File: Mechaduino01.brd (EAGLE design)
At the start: 41.9 x 41.9 mm, 70 parts, among them IC1 SAMD21G18A-AUT, IC2 AP2202-ADJ, Q1 2.5A/30V, Q2 NFET, Q3 BSS138, Q4 BSS138, Q5 BSS138, U3 74AHC1G125, Y1 32,768Khz

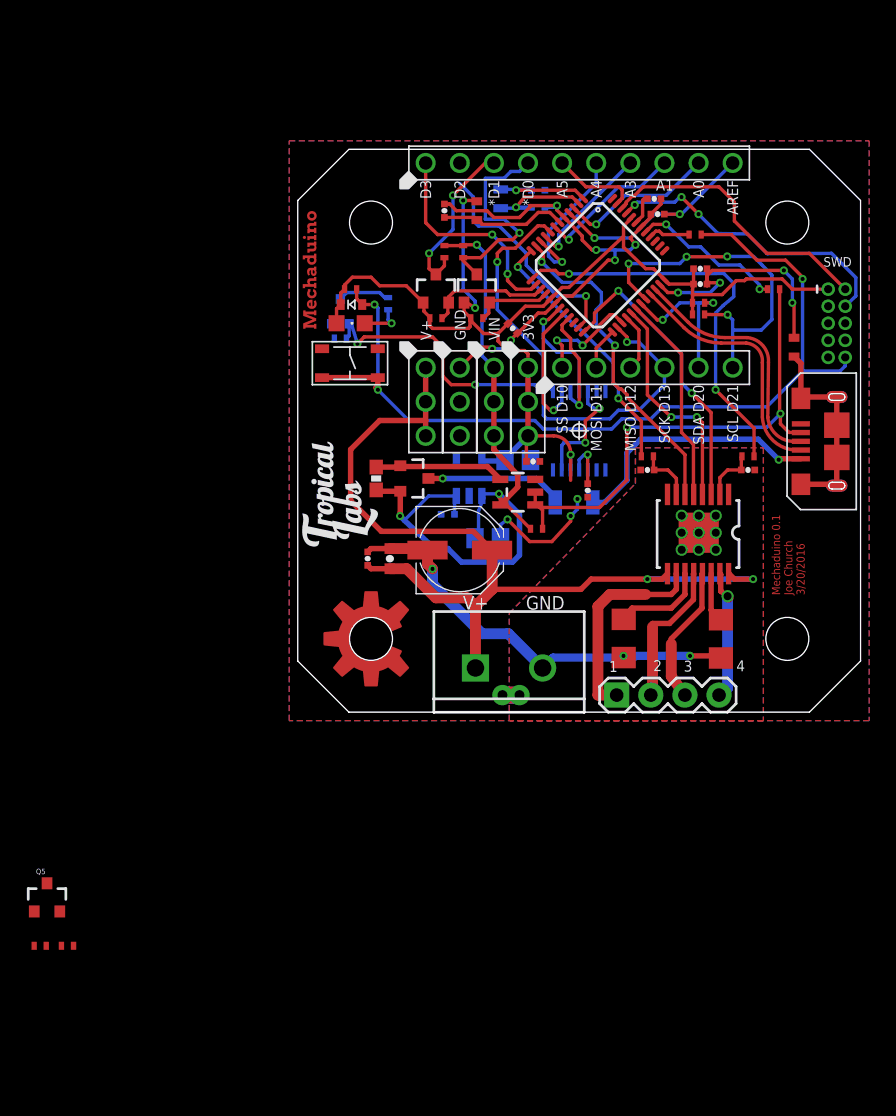
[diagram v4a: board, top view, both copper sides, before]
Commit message: moved IO headers down 0.01
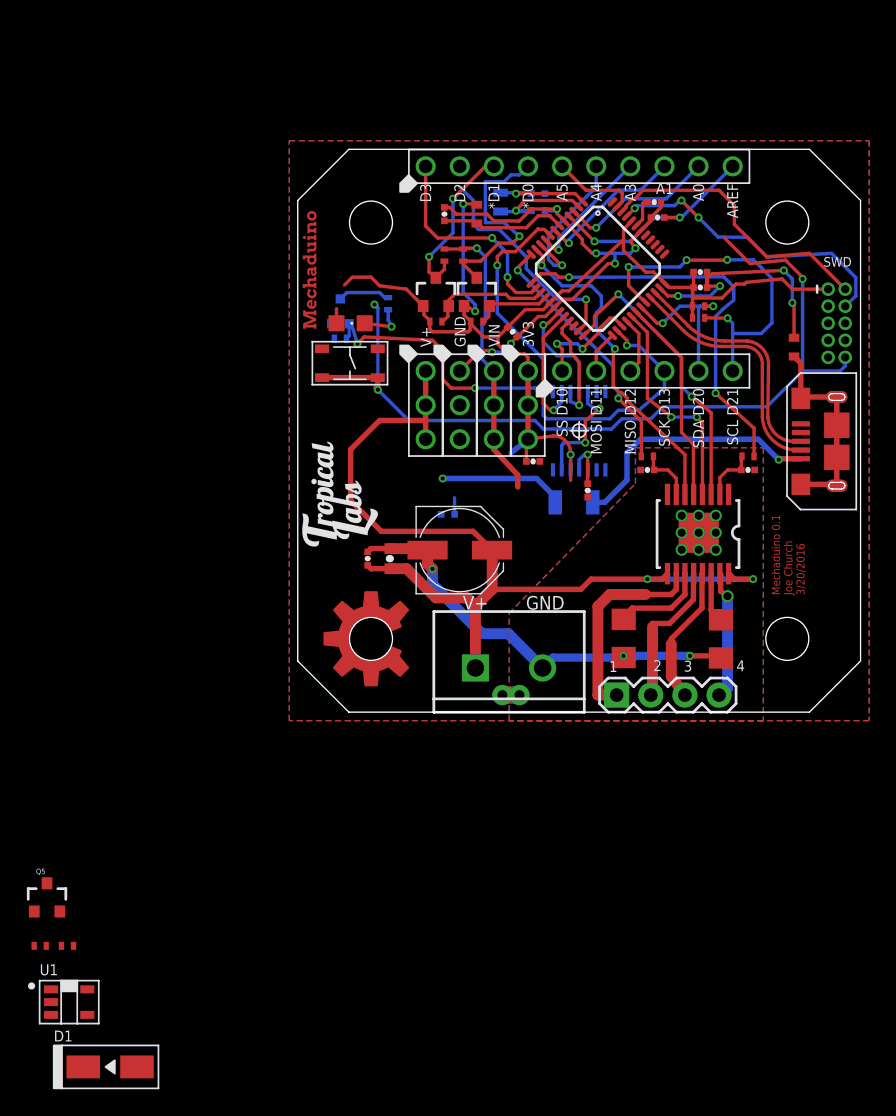
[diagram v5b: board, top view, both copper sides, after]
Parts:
- removed C10, C18: 10.0uF, rcl:C0805
- removed IC2: AP2202-ADJ, SparkFun-PowerIC:SOT23-5$1
- removed Q1: 2.5A/30V, SparkFun-DiscreteSemi:SOT23-3
- removed R1, R9: 100K, adafruit:R0402-VISHAY
- removed R10, R6: 330, adafruit:R0402-VISHAY
- removed R19: 47K, SparkFun-Resistors:0603-RES
- removed U3: 74AHC1G125, SparkFun-DigitalIC:SOT23-5
- added U1: TLV70233PDBVR, MF_IC_Power:SOT-23-5
- C19, C9: value 0.1uF -> 1.0uF
- D1: device adafruit:SOD-523 -> MF_Discrete_Semiconductor:SMA
- moved D1 59.5 mm to (-14.0, -26.4), turned to 0 degrees
- moved C2 0.25 mm to (30.0, 32.8)
- moved C4 0.25 mm to (26.8, 36.8)
- moved C7 0.25 mm to (17.9, 38.6)
- moved 3V3 0.25 mm to (17.1, 22.9)
- moved GND 0.25 mm to (12.1, 22.9)
- moved J3 0.25 mm to (26.0, 25.4)
- moved R20 0.25 mm to (10.3, 29.1)
- moved R3 0.25 mm to (13.3, 29.1)
- moved R8 0.25 mm to (29.8, 30.2)
- moved V+ 0.25 mm to (9.53, 22.9)
- moved VIN 0.25 mm to (14.6, 22.9)
- moved C1 0.25 mm to (30.0, 31.6)
- moved C11 0.25 mm to (26.5, 38.0)
- moved C3 0.25 mm to (16.0, 28.3)
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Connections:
- removed net N$34: Q1.1, R19.1, U3.4
- removed net TARGET_RESET_EDBG: IC1.40, R6.1
- net 3.3V: now also U1.P$5; no longer C10.1, D1.K, IC2.5, R1.2
- net GND: now also U1.P$2; no longer C10.2, C18.2, IC2.2, U3.3
- net N$33: now also D1.ANODE; no longer Q1.3
- net N$7: no longer R10.1, R9.1, U3.1, U3.2
- net PA28_USB_HOST_EN: no longer R10.2
- net RESET: now also IC1.40; no longer D1.A, R1.1, R6.2
- net VIN: now also D1.CATHODE, U1.P$1, U1.P$3; no longer C18.1, IC2.1, IC2.3, Q1.2, R19.2, R9.2, U3.5
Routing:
- net N$7: track 38.0 -> 0.00 mm, vias 2 -> 0
- net VIN: track 58.5 -> 22.9 mm, vias 3 -> 1
- net PA28_USB_HOST_EN: track 11.5 -> 0.00 mm, vias 2 -> 0
- net N$34: track 10.3 -> 0.00 mm
- net GND: track 76.0 -> 66.3 mm, vias 15 -> 12
- net 3.3V: track 91.8 -> 86.9 mm
- net RESET: track 68.4 -> 64.4 mm
- net TARGET_RESET_EDBG: track 3.15 -> 0.00 mm
- net N$33: track 10.4 -> 9.34 mm

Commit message: moved things around
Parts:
- D1: device MF_Discrete_Semiconductor:SMA -> MF_Discrete_Semiconductor:SOD-123
- moved R11 59.8 mm to (10.9, 35.4), turned to 270 degrees
- moved R4 56.0 mm to (9.65, 30.6), turned to 180 degrees
- moved Q5 54.5 mm to (9.65, 32.8)
- moved D1 50.8 mm to (18.7, 12.6), turned to 46.8 degrees
- moved U1 50.6 mm to (16.6, 16.3)
- moved C6 8.39 mm to (10.5, 17.9), turned to 0 degrees
- moved C5 7.19 mm to (17.8, 34.9), turned to 180 degrees
- moved C13 6.17 mm to (10.5, 16.4), turned to 0 degrees
- moved L2 4.51 mm to (17.8, 36.3), turned to 0 degrees
- moved C3 3.49 mm to (19.4, 29.0)
- moved R8 3.25 mm to (28.2, 27.4), turned to 90 degrees
- moved R21 2.85 mm to (13.3, 35.6)
- moved R2 2.85 mm to (14.7, 35.6)
- moved R20 2.85 mm to (12.7, 30.6)
- moved R3 2.85 mm to (15.7, 30.6)
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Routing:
- net 3.3V: track 86.9 -> 1.62 mm, vias 4 -> 0
- net GND: track 66.3 -> 0.00 mm, vias 12 -> 0
- net RESET: track 64.4 -> 0.00 mm, vias 3 -> 0
- net V+: track 69.4 -> 16.8 mm
- net ARDUINO_D13_SCK: track 37.5 -> 0.00 mm, vias 3 -> 0
- net ARDUINO_D4----VREF2: track 30.3 -> 0.00 mm, vias 2 -> 0
- net ARDUINO_D21_SCL: track 27.0 -> 0.00 mm, vias 4 -> 0
- net GND2: track 33.4 -> 8.24 mm, vias 12 -> 11
- net ARDUINO_D8----IN1: track 24.8 -> 0.01 mm, vias 2 -> 0
- net VIN: track 22.9 -> 0.00 mm, vias 1 -> 0
- net PA30_SWCLK: track 22.5 -> 0.00 mm, vias 3 -> 0
- net ARDUINO_D5----IN3: track 22.1 -> 0.00 mm, vias 2 -> 0
- net PA31_SWDIO: track 21.3 -> 0.00 mm
- net ARDUINO_D9----VREF1: track 19.3 -> 0.00 mm, vias 2 -> 0
- net N$36: track 19.3 -> 1.68 mm
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
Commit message: commit after rollback issues
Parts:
- added Q1: BSS138, SparkFun:SOT23-3
- added R1, R6: 10K, adafruit:R0402-VISHAY
- moved C3 0.46 mm to (19.2, 29.3)
- moved J2 0.13 mm to (21.0, 40.8)
- moved J3 0.13 mm to (26.0, 25.5)
- moved 3V3 0.13 mm to (17.1, 23.0)
- moved GND 0.13 mm to (12.1, 23.0)
- moved V+ 0.13 mm to (9.53, 23.0)
- moved VIN 0.13 mm to (14.6, 23.0)
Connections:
- new net HV4: J2.P$1, Q1.3, R6.1
- net 3.3V: now also Q1.1, R1.2
- net ARDUINO_D3: now also Q1.2, R1.1; no longer J2.P$1
- net VIN: now also R6.2
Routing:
- net ARDUINO_D8----IN1: track 0.01 -> 21.9 mm, vias 0 -> 2
- net ARDUINO_D5----IN3: track 0.00 -> 15.1 mm
- net ARDUINO_D6----IN4: track 0.00 -> 15.0 mm, vias 0 -> 2
- net ARDUINO_D7----IN2: track 0.08 -> 14.5 mm, vias 0 -> 2
- net ARDUINO_A2----HEADER_SS: track 0.00 -> 12.8 mm, vias 0 -> 1
- net HEADER_SCK: track 0.00 -> 8.58 mm, vias 0 -> 1
- net HEADER_MISO: track 0.00 -> 6.96 mm, vias 0 -> 1
- net HEADER_MOSI: track 0.00 -> 6.88 mm, vias 0 -> 1
- net RESET: track 0.00 -> 4.15 mm
- net 3.3V: track 1.62 -> 0.00 mm

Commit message: almost completely routed
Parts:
- moved SW2 31.9 mm to (35.4, 31.4), turned to 0 degrees
- moved Q1 17.0 mm to (7.75, 31.9)
- moved R1 15.6 mm to (7.62, 29.7), turned to 180 degrees
- moved R6 9.98 mm to (10.4, 35.8), turned to 270 degrees
- moved C4 2.22 mm to (31.1, 38.0)
- moved C11 2.16 mm to (29.5, 37.3)
- moved C2 2.16 mm to (31.1, 31.0)
- moved R8 1.92 mm to (30.1, 27.7)
- moved C1 1.83 mm to (31.1, 32.1), turned to 180 degrees
- moved R11 1.45 mm to (12.3, 35.8)
- moved R7 1.43 mm to (29.6, 28.8), turned to 0 degrees
- moved R2 1.42 mm to (16.1, 35.8), turned to 270 degrees
- moved C3 1.27 mm to (20.4, 29.3)
- moved IC1 1.25 mm to (24.8, 33.0)
- moved Q3 1.17 mm to (13.8, 33.0)
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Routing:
- net 3.3V: track 0.00 -> 88.4 mm, vias 0 -> 6
- net GND: track 0.00 -> 53.4 mm, vias 0 -> 7
- net ARDUINO_D13_SCK: track 0.00 -> 44.1 mm, vias 0 -> 2
- net VIN: track 0.00 -> 37.9 mm, vias 0 -> 1
- net ARDUINO_D9----VREF1: track 0.00 -> 37.1 mm, vias 0 -> 2
- net V+: track 16.8 -> 51.6 mm
- net ARDUINO_D4----VREF2: track 0.00 -> 26.1 mm, vias 0 -> 2
- net PA30_SWCLK: track 0.00 -> 19.9 mm, vias 0 -> 1
- net PA31_SWDIO: track 0.00 -> 18.1 mm, vias 0 -> 1
- net GND2: track 8.24 -> 25.7 mm, vias 11 -> 12
- net N$36: track 1.67 -> 19.0 mm
- net ARDUINO_D2: track 0.00 -> 17.1 mm, vias 0 -> 2
- net RESET: track 4.15 -> 21.1 mm
- net ARDUINO_D3: track 0.00 -> 14.1 mm, vias 0 -> 2
- net ARDUINO_A4: track 0.00 -> 13.0 mm, vias 0 -> 2
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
